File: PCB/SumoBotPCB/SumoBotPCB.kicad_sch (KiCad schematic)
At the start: 27 parts, among them M1 Motor_DC, M2 Motor_DC, M3 Motor_DC, M4 Motor_DC, SW1 SW_Push, U1 TB6612FNG, U10 VL53L0X-GY530, U11 VL53L0X-GY530, U12 VL53L0X-GY530, U2 hc-05_BLUETOOTH_MODULE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

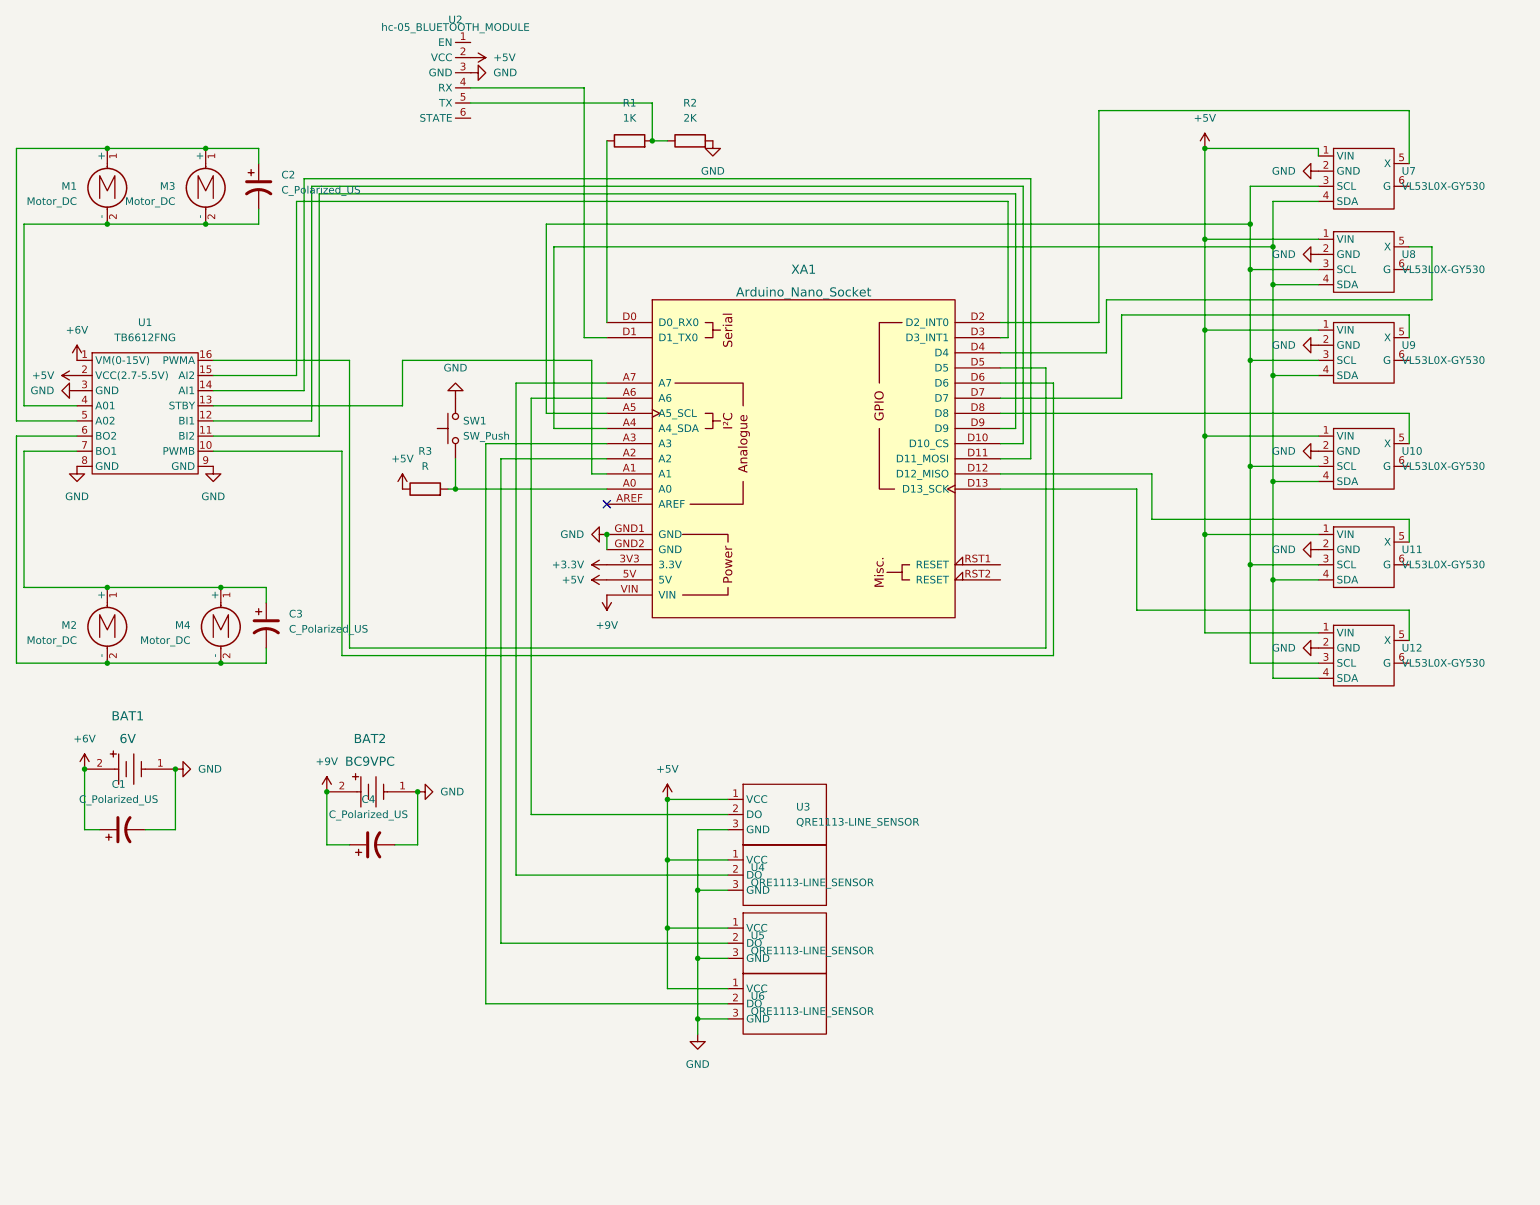
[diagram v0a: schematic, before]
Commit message: corrected driver foot print, add code
corrected footpring of motor driver from being 0.5" to 0.6"  and added the finalized code that works with arduino ide.
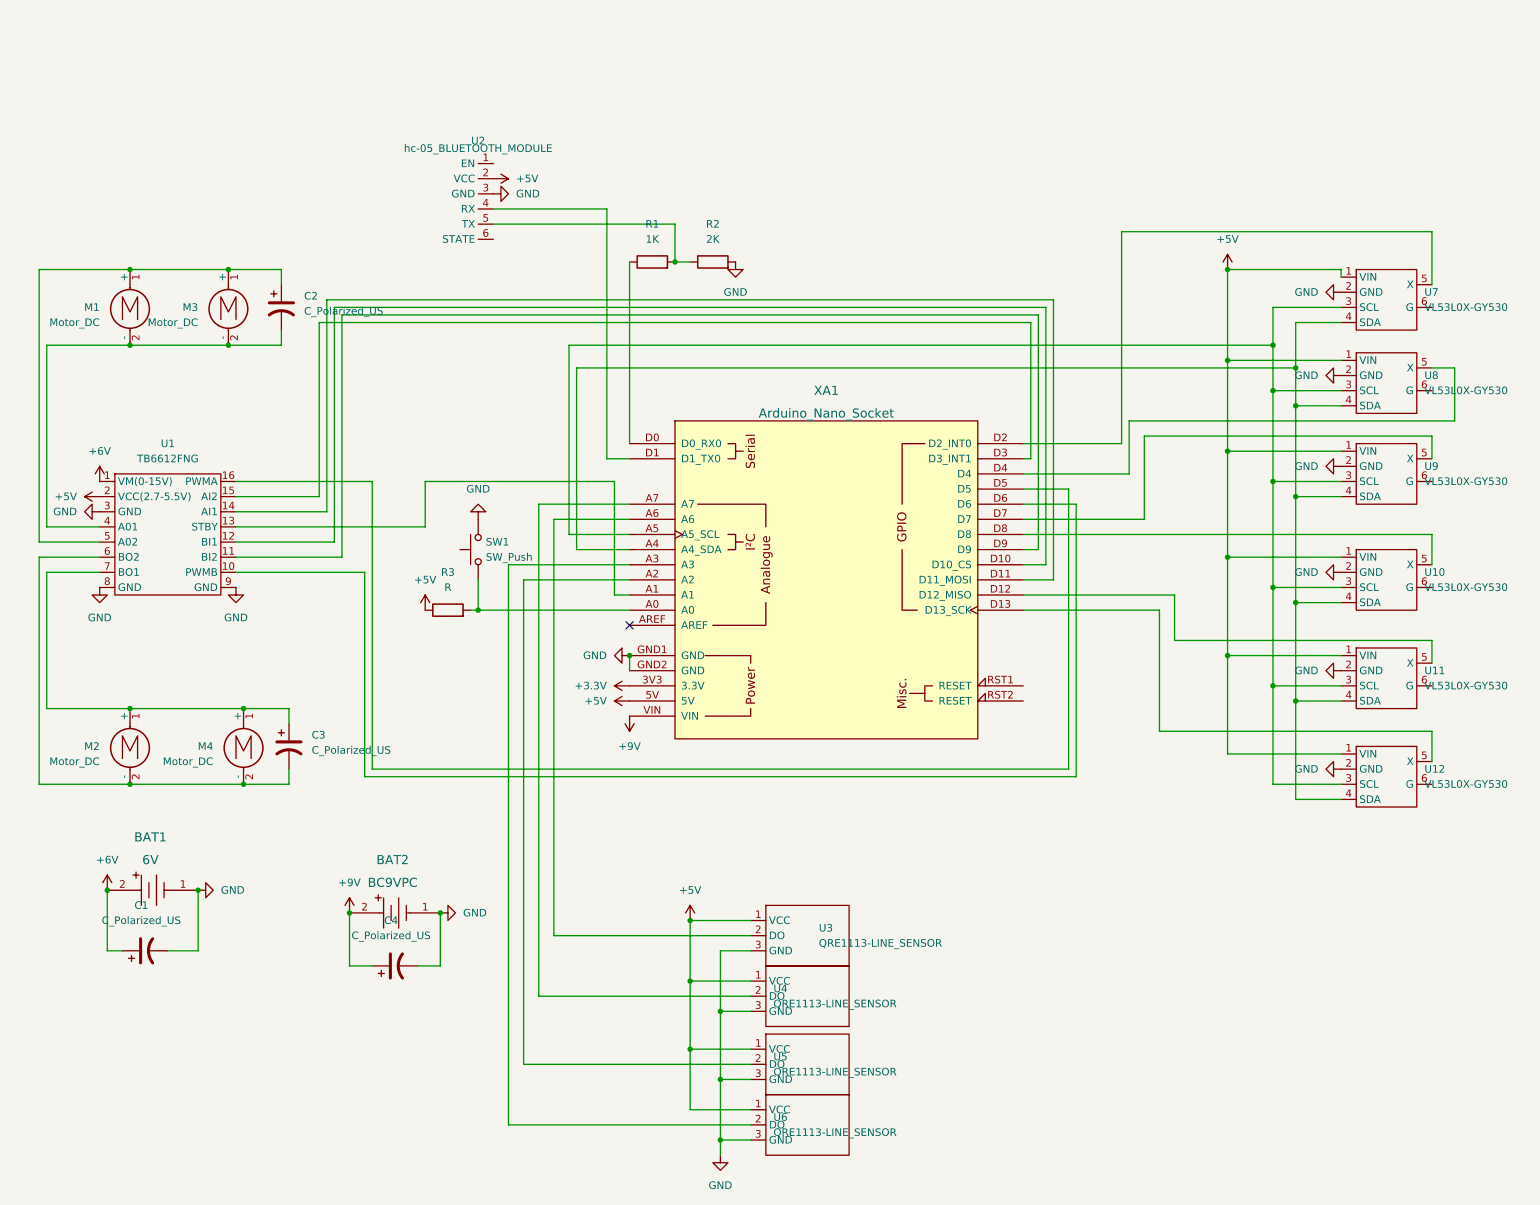
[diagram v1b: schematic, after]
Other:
- moved on the sheet: BAT1, BAT2, C1, C2, C3, C4, M1, M2, M3, M4, R1, R2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
